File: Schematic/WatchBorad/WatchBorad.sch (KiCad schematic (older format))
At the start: 49 parts, among them IC1 TXS0108E, J1 Conn_01x06_Male, J2 Conn_01x09_Female, J3 USB_B_Mini, J4 Conn_01x10_Female, J5 Conn_01x06_Female, J6 Conn_01x04_Male, J7 Conn_01x11_Female, J8 Conn_01x11_Female, J9 Conn_01x12_Female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

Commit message: Draft of PCB routing [PCB]
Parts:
- added L1: 15nH, Inductor_SMD:L_0805_2012Metric_Pad1.15x1.40mm_HandSolder, symbol Device:L
- added L2: 10uH, Inductor_SMD:L_0805_2012Metric_Pad1.15x1.40mm_HandSolder, symbol Device:L
- gave numbers to parts that had none: 4
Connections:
- net labels added: DFU, P_02, P_09, P_10, P_15, P_16, P_17, P_19, P_22, P_23, P_24, P_25
- net labels removed: P_05, P_DCC, P_DEC1, P_DEC2, P_DEC3, P_DEC4
- wire segments 260 -> 305
- no-connect marks 0 -> 3
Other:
- moved on the sheet: J9

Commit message: Routed MAX30102, routed Buttons [PCB]
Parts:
- added J10: Conn_01x07_Female, Connector_PinSocket_2.54mm:PinSocket_1x07_P2.54mm_Vertical, symbol Connector:Conn_01x07_Female
- added R12, R13, R14: 4.7k, Resistor_SMD:R_0805_2012Metric, symbol Device:R
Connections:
- net labels added: HEART_INT, HEART_IRD, HEART_RD, HEART_SCL, HEART_SDA
- net labels removed: P_22, P_23, P_24
- wire segments 305 -> 333
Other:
- note added: "External sockets"
- note added: "MAX30102 Heartrate"
- moved on the sheet: J9, R9, RESET1

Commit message: Moved tisplay on the top of the board[PCB]
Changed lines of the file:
@@
 EESchema Schematic File Version 4
 LIBS:WatchBorad-cache
-EELAYER 26 0
+EELAYER 30 0
 EELAYER END
 $Descr A3 16535 11693
@@
 	8500 1250 9150 1250
 Connection ~ 9150 1250
+Text Label 8600 1950 0    50   ~ 0
+DISP_RS
+Text Label 8600 1850 0    50   ~ 0
+DISP_SDA
+Text Label 8600 1750 0    50   ~ 0
+DISP_SCLK
+Text Label 8600 1650 0    50   ~ 0
+DISP_FMARK
+Text Label 8600 1550 0    50   ~ 0
+DISP_CS
 Text Label 8600 1450 0    50   ~ 0
-DISP_RS
-Text Label 8600 1550 0    50   ~ 0
-DISP_SDA
-Text Label 8600 1650 0    50   ~ 0
-DISP_SCLK
-Text Label 8600 1750 0    50   ~ 0
-DISP_FMARK
-Text Label 8600 1850 0    50   ~ 0
-DISP_CS
-Text Label 8600 1950 0    50   ~ 0
 DISP_RESET
 Wire Wire Line

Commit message: Added P_19 as button SW4
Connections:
- wire segments 333 -> 334
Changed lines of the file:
@@
 Wire Wire Line
 	3900 10250 4350 10250
+Text Label 4350 10950 0    50   ~ 0
+P_19
+Wire Wire Line
+	4350 10950 4200 10950
+Connection ~ 4200 10950
 $EndSCHEMATC

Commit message: Fixed routing for display connector [PCB]
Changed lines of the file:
@@
 Wire Wire Line
 	7300 2150 7050 2150
+Text Label 7050 1950 2    50   ~ 0
+RS_1.8
+Text Label 7050 1850 2    50   ~ 0
+SDA_1.8
+Text Label 7050 1750 2    50   ~ 0
+SCLK_1.8
+Text Label 7050 1650 2    50   ~ 0
+FMARK_1.8
+Text Label 7050 1550 2    50   ~ 0
+CS_1.8
 Text Label 7050 1450 2    50   ~ 0
-RS_1.8
-Text Label 7050 1550 2    50   ~ 0
-SDA_1.8
-Text Label 7050 1650 2    50   ~ 0
-SCLK_1.8
-Text Label 7050 1750 2    50   ~ 0
-FMARK_1.8
-Text Label 7050 1850 2    50   ~ 0
-CS_1.8
-Text Label 7050 1950 2    50   ~ 0
 RESET_1.8
 $Comp

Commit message: Increased capacitors for LDO 3V3 [PCB]
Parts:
- removed C10, C9: 0.1uF, Capacitor_SMD:C_0805_2012Metric_Pad1.15x1.40mm_HandSolder, symbol Device:C
- added C5, C6: 10uF, Capacitor_SMD:CP_Elec_4x3.9, symbol Device:CP
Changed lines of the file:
@@
 EESchema Schematic File Version 4
 LIBS:WatchBorad-cache
-EELAYER 30 0
+EELAYER 26 0
 EELAYER END
 $Descr A3 16535 11693
@@
 $EndComp
 $Comp
-L Device:C C10
-U 1 1 5DB89395
-P 2050 8350
-F 0 "C10" H 2165 8396 50  0000 L CNN
-F 1 "0.1uF" H 2165 8305 50  0000 L CNN
-F 2 "Capacitor_SMD:C_0805_2012Metric_Pad1.15x1.40mm_HandSolder" H 2088 8200 50  0001 C CNN
-F 3 "~" H 2050 8350 50  0001 C CNN
-	1    2050 8350
-	1    0    0    -1
-$EndComp
-$Comp
 L power:GND #PWR0131
 U 1 1 5DB88504
@@
 Wire Notes Line
 	2450 7700 2450 6300
-$Comp
-L Device:C C9
-U 1 1 5DBC7BF7
-P 1200 8350
-F 0 "C9" H 1315 8396 50  0000 L CNN
-F 1 "0.1uF" H 1315 8305 50  0000 L CNN
-F 2 "Capacitor_SMD:C_0805_2012Metric_Pad1.15x1.40mm_HandSolder" H 1238 8200 50  0001 C CNN
-F 3 "~" H 1200 8350 50  0001 C CNN
-	1    1200 8350
-	1    0    0    -1
-$EndComp
 $Comp
 L power:+5V #PWR0132
@@
 	4350 10950 4200 10950
 Connection ~ 4200 10950
+$Comp
+L Device:CP C6
+U 1 1 5DC2AF23
+P 2050 8350
+F 0 "C6" H 2168 8396 50  0000 L CNN
+F 1 "10uF" H 2168 8305 50  0000 L CNN
+F 2 "Capacitor_SMD:CP_Elec_4x3.9" H 2088 8200 50  0001 C CNN
+F 3 "~" H 2050 8350 50  0001 C CNN
+	1    2050 8350
+	1    0    0    -1
+$EndComp
+$Comp
+L Device:CP C5
+U 1 1 5DC2B18E
+P 1200 8350
+F 0 "C5" H 1318 8396 50  0000 L CNN
+F 1 "10uF" H 1318 8305 50  0000 L CNN
+F 2 "Capacitor_SMD:CP_Elec_4x3.9" H 1238 8200 50  0001 C CNN
+F 3 "~" H 1200 8350 50  0001 C CNN
+	1    1200 8350
+	1    0    0    -1
+$EndComp
 $EndSCHEMATC

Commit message: Added hierarchical sheet with vibration motor circuit
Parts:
- IC1: symbol TXS0108E:TXS0108E -> WatchBorad-rescue:TXS0108E-TXS0108E
- U1: symbol RF_Module:E73-2G4M04S-52832 -> WatchBorad-rescue:E73-2G4M04S-52832-RF_Module
- U2: symbol Hirose_connectors:FH26-13S-0.3SHW(05) -> WatchBorad-rescue:FH26-13S-0.3SHW(05)-Hirose_connectors
- U3: symbol W25Q16BVSSIG:W25Q16BVSSIG -> WatchBorad-rescue:W25Q16BVSSIG-W25Q16BVSSIG
- U8: symbol MPU-9250:MPU-9250 -> WatchBorad-rescue:MPU-9250-MPU-9250
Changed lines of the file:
@@
 EESchema Schematic File Version 4
-LIBS:WatchBorad-cache
-EELAYER 26 0
+EELAYER 30 0
 EELAYER END
 $Descr A3 16535 11693
 encoding utf-8
-Sheet 1 1
+Sheet 1 2
 Title ""
 Date ""
@@
 $EndDescr
 $Comp
-L RF_Module:E73-2G4M04S-52832 U1
+L WatchBorad-rescue:E73-2G4M04S-52832-RF_Module U1
 U 1 1 5D87721B
 P 2600 2950
@@
 $EndComp
 $Comp
-L W25Q16BVSSIG:W25Q16BVSSIG U3
+L WatchBorad-rescue:W25Q16BVSSIG-W25Q16BVSSIG U3
 U 1 1 5D87735B
 P 11650 1500
@@
 $EndComp
 $Comp
-L Hirose_connectors:FH26-13S-0.3SHW(05) U2
+L WatchBorad-rescue:FH26-13S-0.3SHW(05)-Hirose_connectors U2
 U 1 1 5D877F18
 P 8050 3450
@@
 $EndComp
 $Comp
-L TXS0108E:TXS0108E IC1
+L WatchBorad-rescue:TXS0108E-TXS0108E IC1
 U 1 1 5D8780E1
 P 7900 1650
@@
 SPI FLASH Memory\n
 $Comp
-L MPU-9250:MPU-9250 U8
+L WatchBorad-rescue:MPU-9250-MPU-9250 U8
 U 1 1 5DDDC579
 P 7300 5550
@@
 	1    0    0    -1
 $EndComp
+$Sheet
+S 11050 7050 1700 900
+U 5EA4867C
+F0 "VM" 50
+F1 "VibrationMotor.sch" 50
+F2 "VCC_motor" I L 11050 7200 50
+F3 "Enable_motor" I L 11050 7725 50
+$EndSheet
 $EndSCHEMATC

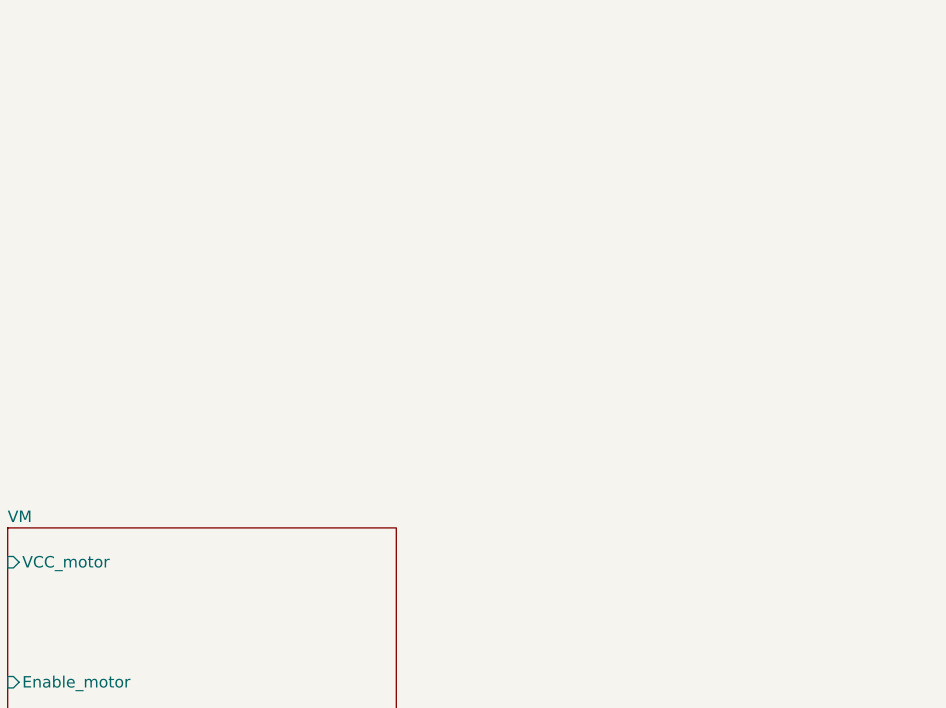
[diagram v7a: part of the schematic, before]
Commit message: Added PowerSupply and MCU hierarchical sheets.
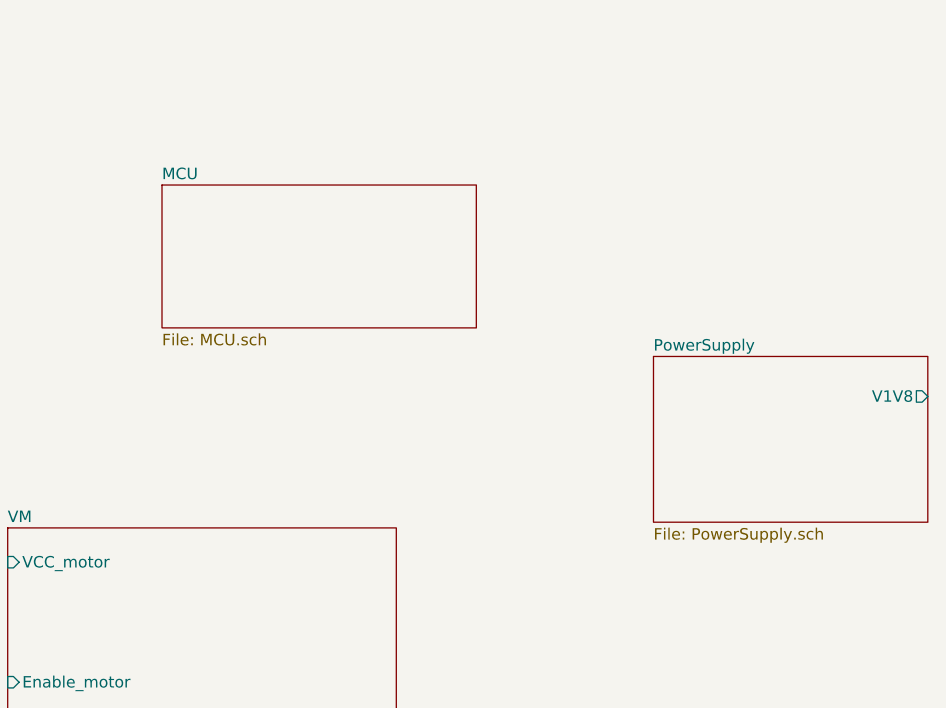
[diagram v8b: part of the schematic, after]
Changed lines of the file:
@@
 $Descr A3 16535 11693
 encoding utf-8
-Sheet 1 2
+Sheet 1 4
 Title ""
 Date ""
@@
 F3 "Enable_motor" I L 11050 7725 50
 $EndSheet
+$Sheet
+S 11725 5550 1375 625
+U 5E9B1DCE
+F0 "MCU" 50
+F1 "MCU.sch" 50
+$EndSheet
+$Sheet
+S 13875 6300 1200 725
+U 5E9C1C3A
+F0 "PowerSupply" 50
+F1 "PowerSupply.sch" 50
+F2 "V1V8" O R 15075 6475 50
+$EndSheet
 $EndSCHEMATC
